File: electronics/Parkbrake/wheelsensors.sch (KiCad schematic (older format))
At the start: 61 parts

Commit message: ordernr, type and footprints for all components
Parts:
- C? (x2): footprint (none) -> Capacitors_SMD:C_0805; farnell (none) -> 2496940; part (none) -> 0805B104J500CT
- C? (x2): value 10n -> 1n; footprint (none) -> Capacitors_SMD:C_0805; farnell (none) -> 2494247; part (none) -> GRM2165C1H102JA01D
- C? (x2): footprint (none) -> Capacitors_SMD:c_elec_5x5.3; symbol C -> CP; farnell (none) -> 1870621; part (none) -> MCESL35V106M5X5.2
- C? (x4): footprint (none) -> Capacitors_SMD:C_0805; farnell (none) -> 2496981; part (none) -> 0805B473J500CT
- C? (x14): footprint (none) -> Capacitors_SMD:C_1206; farnell (none) -> 2362126; part (none) -> GRM31MR71E105JA01L
- Q?: value Q_PMOS_GSD -> BSS308; footprint (none) -> TO_SOT_Packages_SMD:SOT-23; farnell (none) -> 2432719; part (none) -> BSS308PE H6327
- Q?: value BSS138 -> 2N7002; footprint SOT-23 -> TO_SOT_Packages_SMD:SOT-23; farnell (none) -> 1510761; part (none) -> 2N7002
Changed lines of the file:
@@
 F 0 "C?" H 9925 3525 50  0000 L CNN
 F 1 "100n" H 9925 3325 50  0000 L CNN
-F 2 "" H 9938 3275 50  0000 C CNN
+F 2 "Capacitors_SMD:C_0805" H 9938 3275 50  0001 C CNN
 F 3 "" H 9900 3425 50  0000 C CNN
+F 4 "0805B104J500CT" H 9900 3425 60  0001 C CNN "part"
+F 5 "2496940" H 9900 3425 60  0001 C CNN "farnell"
 	1    9900 3425
 	1    0    0    -1
@@
 P 10150 3425
 F 0 "C?" H 10175 3525 50  0000 L CNN
-F 1 "10n" H 10175 3325 50  0000 L CNN
-F 2 "" H 10188 3275 50  0000 C CNN
+F 1 "1n" H 10175 3325 50  0000 L CNN
+F 2 "Capacitors_SMD:C_0805" H 10188 3275 50  0001 C CNN
 F 3 "" H 10150 3425 50  0000 C CNN
+F 4 "GRM2165C1H102JA01D" H 10150 3425 60  0001 C CNN "part"
+F 5 "2494247" H 10150 3425 60  0001 C CNN "farnell"
 	1    10150 3425
 	1    0    0    -1
 $EndComp
 $Comp
-L C C?
+L CP C?
 U 1 1 579010A2
 P 9650 3425
 F 0 "C?" H 9675 3525 50  0000 L CNN
 F 1 "10u" H 9675 3325 50  0000 L CNN
-F 2 "" H 9688 3275 50  0000 C CNN
+F 2 "Capacitors_SMD:c_elec_5x5.3" H 9688 3275 50  0001 C CNN
 F 3 "" H 9650 3425 50  0000 C CNN
+F 4 "1870621" H 9650 3425 60  0001 C CNN "farnell"
+F 5 "MCESL35V106M5X5.2" H 9650 3425 60  0001 C CNN "part"
 	1    9650 3425
 	1    0    0    -1
@@
 F 0 "C?" H 6950 3150 50  0000 L CNN
 F 1 "47n" H 6950 2950 50  0000 L CNN
-F 2 "" H 6963 2900 50  0000 C CNN
+F 2 "Capacitors_SMD:C_0805" H 6963 2900 50  0001 C CNN
 F 3 "" H 6925 3050 50  0000 C CNN
+F 4 "0805B473J500CT" H 6925 3050 60  0001 C CNN "part"
+F 5 "2496981" H 6925 3050 60  0001 C CNN "farnell"
 	1    6925 3050
 	1    0    0    -1
@@
 F 0 "C?" H 7225 3150 50  0000 L CNN
 F 1 "47n" H 7225 2950 50  0000 L CNN
-F 2 "" H 7238 2900 50  0000 C CNN
+F 2 "Capacitors_SMD:C_0805" H 7238 2900 50  0001 C CNN
 F 3 "" H 7200 3050 50  0000 C CNN
+F 4 "0805B473J500CT" H 7200 3050 60  0001 C CNN "part"
+F 5 "2496981" H 7200 3050 60  0001 C CNN "farnell"
 	1    7200 3050
 	1    0    0    -1
@@
 P 10075 4775
 F 0 "Q?" V 10300 4600 50  0000 R CNN
-F 1 "Q_PMOS_GSD" V 10425 5000 50  0000 R CNN
-F 2 "" H 10275 4875 50  0000 C CNN
+F 1 "BSS308" V 10300 4975 50  0000 R CNN
+F 2 "TO_SOT_Packages_SMD:SOT-23" H 10275 4875 50  0001 C CNN
 F 3 "" H 10075 4775 50  0000 C CNN
+F 4 "BSS308PE H6327" V 10075 4775 60  0001 C CNN "part"
+F 5 "2432719" V 10075 4775 60  0001 C CNN "farnell"
 	1    10075 4775
 	0    1    -1   0
@@
 P 9975 5325
 F 0 "Q?" H 10175 5400 50  0000 L CNN
-F 1 "BSS138" H 10175 5325 50  0000 L CNN
-F 2 "SOT-23" H 10175 5250 50  0000 L CIN
+F 1 "2N7002" H 10175 5325 50  0000 L CNN
+F 2 "TO_SOT_Packages_SMD:SOT-23" H 10175 5250 50  0001 L CIN
 F 3 "" H 9975 5325 50  0000 L CNN
+F 4 "1510761" H 9975 5325 60  0001 C CNN "farnell"
+F 5 "2N7002" H 9975 5325 60  0001 C CNN "part"
 	1    9975 5325
 	1    0    0    -1
@@
 F 0 "C?" H 9875 2125 50  0000 L CNN
 F 1 "100n" H 9875 1925 50  0000 L CNN
-F 2 "" H 9888 1875 50  0000 C CNN
+F 2 "Capacitors_SMD:C_0805" H 9888 1875 50  0001 C CNN
 F 3 "" H 9850 2025 50  0000 C CNN
+F 4 "0805B104J500CT" H 9850 2025 60  0001 C CNN "part"
+F 5 "2496940" H 9850 2025 60  0001 C CNN "farnell"
 	1    9850 2025
 	1    0    0    -1
@@
 P 10100 2025
 F 0 "C?" H 10125 2125 50  0000 L CNN
-F 1 "10n" H 10125 1925 50  0000 L CNN
-F 2 "" H 10138 1875 50  0000 C CNN
+F 1 "1n" H 10125 1925 50  0000 L CNN
+F 2 "Capacitors_SMD:C_0805" H 10138 1875 50  0001 C CNN
 F 3 "" H 10100 2025 50  0000 C CNN
+F 4 "GRM2165C1H102JA01D" H 10100 2025 60  0001 C CNN "part"
+F 5 "2494247" H 10100 2025 60  0001 C CNN "farnell"
 	1    10100 2025
 	1    0    0    -1
 $EndComp
 $Comp
-L C C?
+L CP C?
 U 1 1 579039C6
 P 9600 2025
 F 0 "C?" H 9625 2125 50  0000 L CNN
 F 1 "10u" H 9625 1925 50  0000 L CNN
-F 2 "" H 9638 1875 50  0000 C CNN
+F 2 "Capacitors_SMD:c_elec_5x5.3" H 9638 1875 50  0001 C CNN
 F 3 "" H 9600 2025 50  0000 C CNN
+F 4 "1870621" H 9600 2025 60  0001 C CNN "farnell"
+F 5 "MCESL35V106M5X5.2" H 9600 2025 60  0001 C CNN "part"
 	1    9600 2025
 	1    0    0    -1
@@
 F 0 "C?" H 6950 1825 50  0000 L CNN
 F 1 "47n" H 6950 1625 50  0000 L CNN
-F 2 "" H 6963 1575 50  0000 C CNN
+F 2 "Capacitors_SMD:C_0805" H 6963 1575 50  0001 C CNN
 F 3 "" H 6925 1725 50  0000 C CNN
+F 4 "0805B473J500CT" H 6925 1725 60  0001 C CNN "part"
+F 5 "2496981" H 6925 1725 60  0001 C CNN "farnell"
 	1    6925 1725
 	1    0    0    -1
@@
 F 0 "C?" H 7225 1825 50  0000 L CNN
 F 1 "47n" H 7225 1625 50  0000 L CNN
-F 2 "" H 7238 1575 50  0000 C CNN
+F 2 "Capacitors_SMD:C_0805" H 7238 1575 50  0001 C CNN
 F 3 "" H 7200 1725 50  0000 C CNN
+F 4 "0805B473J500CT" H 7200 1725 60  0001 C CNN "part"
+F 5 "2496981" H 7200 1725 60  0001 C CNN "farnell"
 	1    7200 1725
 	1    0    0    -1
@@
 F 0 "C?" H 3250 5200 50  0000 L CNN
 F 1 "1u" H 3250 5000 50  0000 L CNN
-F 2 "" H 3263 4950 50  0000 C CNN
+F 2 "Capacitors_SMD:C_1206" H 3263 4950 50  0001 C CNN
 F 3 "" H 3225 5100 50  0000 C CNN
+F 4 "2362126" H 3225 5100 60  0001 C CNN "farnell"
+F 5 "GRM31MR71E105JA01L" H 3225 5100 60  0001 C CNN "part"
 	1    3225 5100
 	1    0    0    -1
@@
 F 0 "C?" H 3100 5450 50  0000 L CNN
 F 1 "1u" H 3100 5250 50  0000 L CNN
-F 2 "" H 3113 5200 50  0000 C CNN
+F 2 "Capacitors_SMD:C_1206" H 3113 5200 50  0001 C CNN
 F 3 "" H 3075 5350 50  0000 C CNN
+F 4 "2362126" H 3075 5350 60  0001 C CNN "farnell"
+F 5 "GRM31MR71E105JA01L" H 3075 5350 60  0001 C CNN "part"
 	1    3075 5350
 	0    1    1    0
@@
 F 0 "C?" H 3100 5950 50  0000 L CNN
 F 1 "1u" H 3100 5750 50  0000 L CNN
-F 2 "" H 3113 5700 50  0000 C CNN
+F 2 "Capacitors_SMD:C_1206" H 3113 5700 50  0001 C CNN
 F 3 "" H 3075 5850 50  0000 C CNN
+F 4 "2362126" H 3075 5850 60  0001 C CNN "farnell"
+F 5 "GRM31MR71E105JA01L" H 3075 5850 60  0001 C CNN "part"
 	1    3075 5850
 	0    1    1    0
@@
 F 0 "C?" H 1600 5250 50  0000 L CNN
 F 1 "1u" H 1600 5050 50  0000 L CNN
-F 2 "" H 1613 5000 50  0000 C CNN
+F 2 "Capacitors_SMD:C_1206" H 1613 5000 50  0001 C CNN
 F 3 "" H 1575 5150 50  0000 C CNN
+F 4 "2362126" H 1575 5150 60  0001 C CNN "farnell"
+F 5 "GRM31MR71E105JA01L" H 1575 5150 60  0001 C CNN "part"
 	1    1575 5150
 	1    0    0    -1
@@
 F 0 "C?" H 1600 5750 50  0000 L CNN
 F 1 "1u" H 1600 5550 50  0000 L CNN
-F 2 "" H 1613 5500 50  0000 C CNN
+F 2 "Capacitors_SMD:C_1206" H 1613 5500 50  0001 C CNN
 F 3 "" H 1575 5650 50  0000 C CNN
+F 4 "2362126" H 1575 5650 60  0001 C CNN "farnell"
+F 5 "GRM31MR71E105JA01L" H 1575 5650 60  0001 C CNN "part"
 	1    1575 5650
 	1    0    0    -1
@@
 F 0 "C?" H 3150 6400 50  0000 L CNN
 F 1 "1u" H 3150 6200 50  0000 L CNN
-F 2 "" H 3163 6150 50  0000 C CNN
+F 2 "Capacitors_SMD:C_1206" H 3163 6150 50  0001 C CNN
 F 3 "" H 3125 6300 50  0000 C CNN
+F 4 "2362126" H 3125 6300 60  0001 C CNN "farnell"
+F 5 "GRM31MR71E105JA01L" H 3125 6300 60  0001 C CNN "part"
 	1    3125 6300
 	1    0    0    -1
@@
 F 0 "C?" H 3375 6400 50  0000 L CNN
 F 1 "1u" H 3375 6200 50  0000 L CNN
-F 2 "" H 3388 6150 50  0000 C CNN
+F 2 "Capacitors_SMD:C_1206" H 3388 6150 50  0001 C CNN
 F 3 "" H 3350 6300 50  0000 C CNN
+F 4 "2362126" H 3350 6300 60  0001 C CNN "farnell"
+F 5 "GRM31MR71E105JA01L" H 3350 6300 60  0001 C CNN "part"
 	1    3350 6300
 	1    0    0    -1
@@
 F 0 "C?" H 6300 5200 50  0000 L CNN
 F 1 "1u" H 6300 5000 50  0000 L CNN
-F 2 "" H 6313 4950 50  0000 C CNN
+F 2 "Capacitors_SMD:C_1206" H 6313 4950 50  0001 C CNN
 F 3 "" H 6275 5100 50  0000 C CNN
+F 4 "2362126" H 6275 5100 60  0001 C CNN "farnell"
+F 5 "GRM31MR71E105JA01L" H 6275 5100 60  0001 C CNN "part"
 	1    6275 5100
 	1    0    0    -1
@@
 F 0 "C?" H 6150 5450 50  0000 L CNN
 F 1 "1u" H 6150 5250 50  0000 L CNN
-F 2 "" H 6163 5200 50  0000 C CNN
+F 2 "Capacitors_SMD:C_1206" H 6163 5200 50  0001 C CNN
 F 3 "" H 6125 5350 50  0000 C CNN
+F 4 "2362126" H 6125 5350 60  0001 C CNN "farnell"
+F 5 "GRM31MR71E105JA01L" H 6125 5350 60  0001 C CNN "part"
 	1    6125 5350
 	0    1    1    0
@@
 F 0 "C?" H 6150 5950 50  0000 L CNN
 F 1 "1u" H 6150 5750 50  0000 L CNN
-F 2 "" H 6163 5700 50  0000 C CNN
+F 2 "Capacitors_SMD:C_1206" H 6163 5700 50  0001 C CNN
 F 3 "" H 6125 5850 50  0000 C CNN
+F 4 "2362126" H 6125 5850 60  0001 C CNN "farnell"
+F 5 "GRM31MR71E105JA01L" H 6125 5850 60  0001 C CNN "part"
 	1    6125 5850
 	0    1    1    0
@@
 F 0 "C?" H 4650 5250 50  0000 L CNN
 F 1 "1u" H 4650 5050 50  0000 L CNN
-F 2 "" H 4663 5000 50  0000 C CNN
+F 2 "Capacitors_SMD:C_1206" H 4663 5000 50  0001 C CNN
 F 3 "" H 4625 5150 50  0000 C CNN
+F 4 "2362126" H 4625 5150 60  0001 C CNN "farnell"
+F 5 "GRM31MR71E105JA01L" H 4625 5150 60  0001 C CNN "part"
 	1    4625 5150
 	1    0    0    -1
@@
 F 0 "C?" H 4650 5750 50  0000 L CNN
 F 1 "1u" H 4650 5550 50  0000 L CNN
-F 2 "" H 4663 5500 50  0000 C CNN
+F 2 "Capacitors_SMD:C_1206" H 4663 5500 50  0001 C CNN
 F 3 "" H 4625 5650 50  0000 C CNN
+F 4 "2362126" H 4625 5650 60  0001 C CNN "farnell"
+F 5 "GRM31MR71E105JA01L" H 4625 5650 60  0001 C CNN "part"
 	1    4625 5650
 	1    0    0    -1
@@
 F 0 "C?" H 6200 6400 50  0000 L CNN
 F 1 "1u" H 6200 6200 50  0000 L CNN
-F 2 "" H 6213 6150 50  0000 C CNN
+F 2 "Capacitors_SMD:C_1206" H 6213 6150 50  0001 C CNN
 F 3 "" H 6175 6300 50  0000 C CNN
+F 4 "2362126" H 6175 6300 60  0001 C CNN "farnell"
+F 5 "GRM31MR71E105JA01L" H 6175 6300 60  0001 C CNN "part"
 	1    6175 6300
 	1    0    0    -1
@@
 F 0 "C?" H 6425 6400 50  0000 L CNN
 F 1 "1u" H 6425 6200 50  0000 L CNN
-F 2 "" H 6438 6150 50  0000 C CNN
+F 2 "Capacitors_SMD:C_1206" H 6438 6150 50  0001 C CNN
 F 3 "" H 6400 6300 50  0000 C CNN
+F 4 "2362126" H 6400 6300 60  0001 C CNN "farnell"
+F 5 "GRM31MR71E105JA01L" H 6400 6300 60  0001 C CNN "part"
 	1    6400 6300
 	1    0    0    -1

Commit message: Make it pass DRC rule check
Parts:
- gave numbers to parts that had none: 61

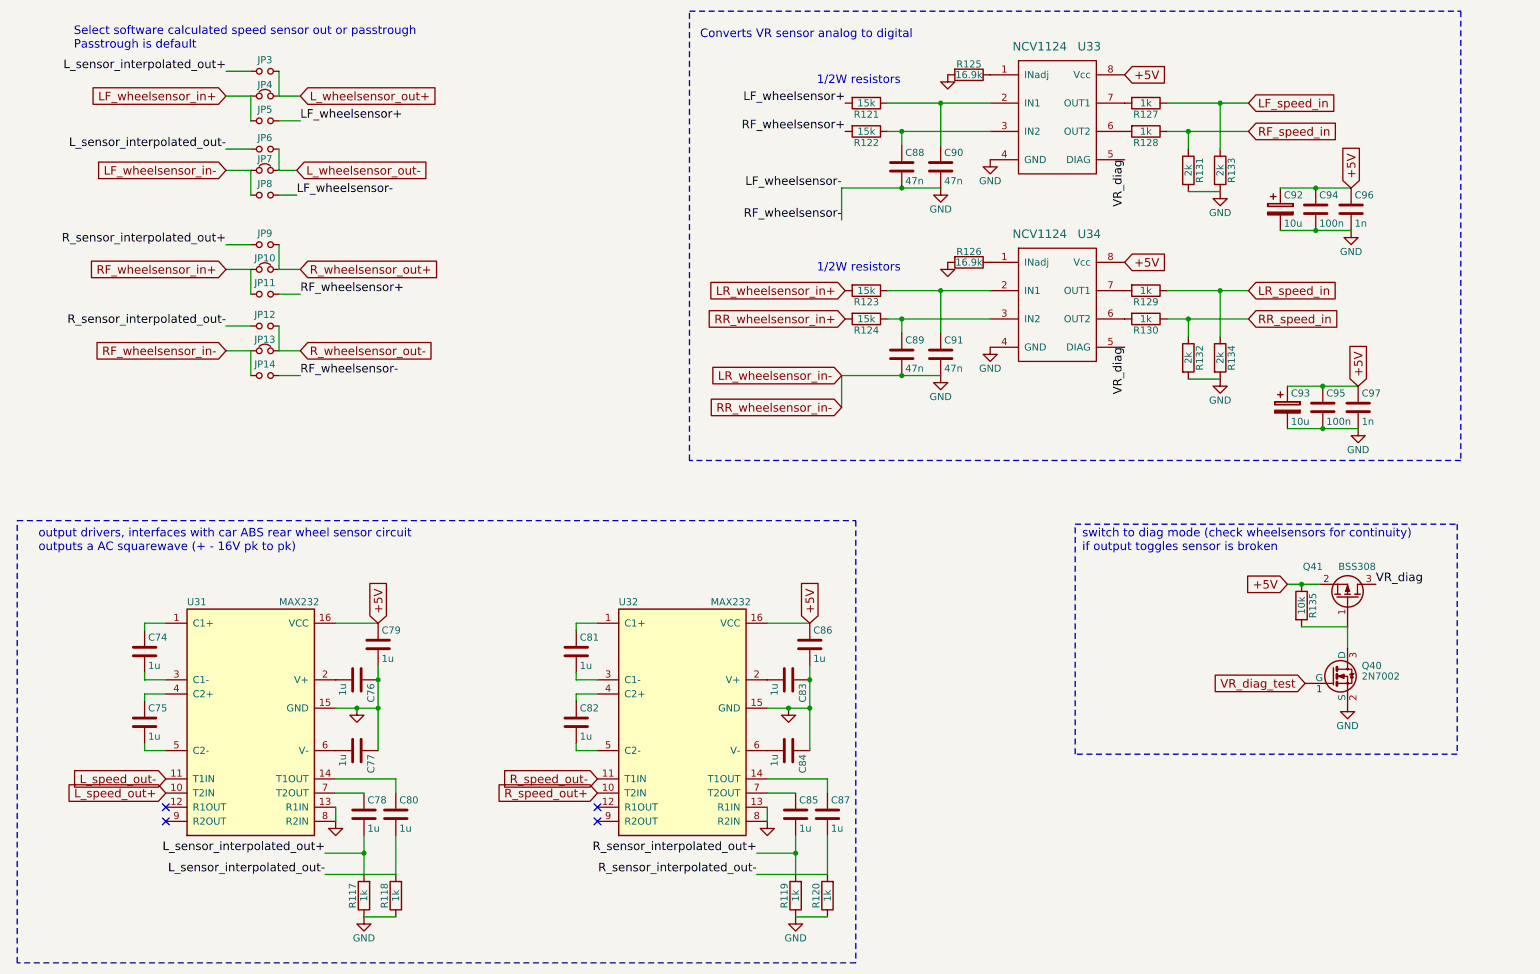
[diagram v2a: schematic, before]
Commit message: More fixes and chenged components eat less boardspace
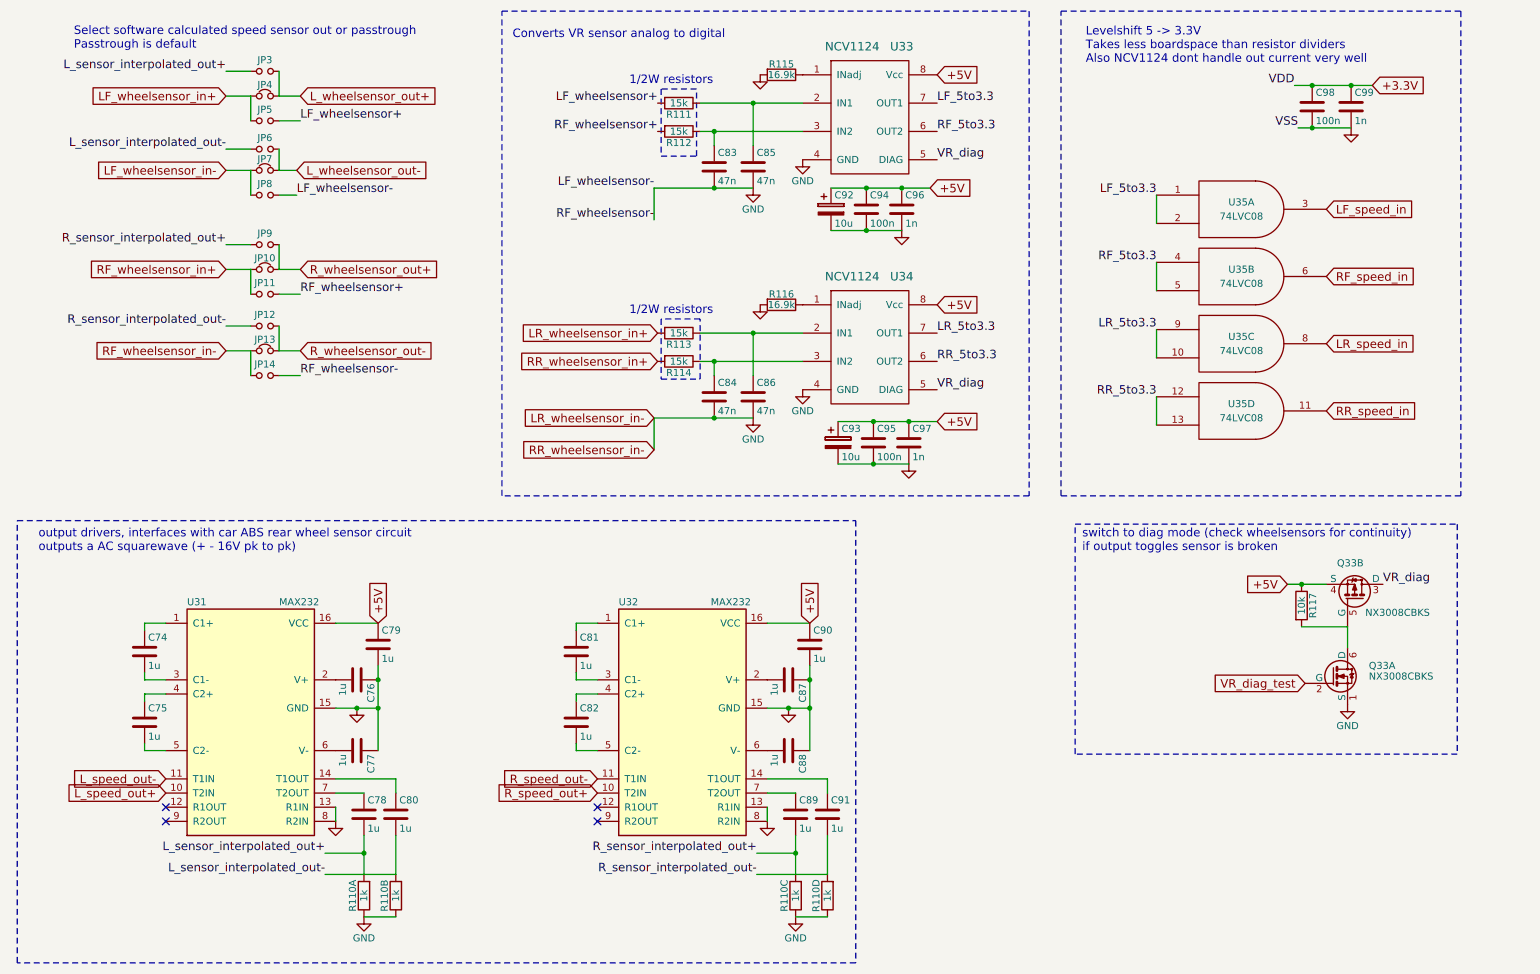
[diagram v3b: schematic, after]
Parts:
- removed Q40: 2N7002, TO_SOT_Packages_SMD:SOT-23, symbol BSS138
- removed Q41: BSS308, TO_SOT_Packages_SMD:SOT-23, symbol Q_PMOS_GSD
- removed R117, R118, R119, R120, R127, R128, R129, R130: 1k, Resistors_SMD:R_0805, symbol R
- removed R131, R132, R133, R134: 2k, Resistors_SMD:R_0805, symbol R
- added C98: 100n, Capacitors_SMD:C_0805, symbol C
- added C99: 1n, Capacitors_SMD:C_0805, symbol C
- added Q33: NX3008CBKS, SOT363:SOT-363, symbol NX3008CBKS
- added R110: 1k, Resistors_SMD:R_Array_Concave_4x0603, symbol Rnet4
- added U35: 74LVC08, Housings_SSOP:TSSOP-14_4.4x5mm_Pitch0.65mm, symbol 74LS08
- C92, C93: footprint Capacitors_SMD:c_elec_5x5.3 -> myfootprints:CP_0805; farnell 1870621 -> 2491430; part MCESL35V106M5X5.2 -> TMCP0J106KTRF
- JP10: value Jumper_NC_Small -> RF_passth+; footprint (none) -> Resistors_SMD:R_0805_HandSoldering; farnell (none) -> 9240276; part (none) -> RC1206JR-070RL
- JP11: value Jumper_NO_Small -> RF+_to_in; footprint (none) -> Resistors_SMD:R_0805_HandSoldering; farnell (none) -> 9240276; part (none) -> RC1206JR-070RL
- JP12: value Jumper_NO_Small -> soft_R_out-; footprint (none) -> Resistors_SMD:R_0805_HandSoldering; farnell (none) -> 9240276; part (none) -> RC1206JR-070RL
- JP13: value Jumper_NC_Small -> RF_passth-; footprint (none) -> Resistors_SMD:R_0805_HandSoldering; farnell (none) -> 9240276; part (none) -> RC1206JR-070RL
- JP14: value Jumper_NO_Small -> RF-_to_in; footprint (none) -> Resistors_SMD:R_0805_HandSoldering; farnell (none) -> 9240276; part (none) -> RC1206JR-070RL
- JP3: value Jumper_NO_Small -> soft_L_out+; footprint (none) -> Resistors_SMD:R_0805_HandSoldering; farnell (none) -> 9240276; part (none) -> RC1206JR-070RL
- JP4: value Jumper_NC_Small -> L_passth+; footprint (none) -> Resistors_SMD:R_0805_HandSoldering; farnell (none) -> 9240276; part (none) -> RC1206JR-070RL
- JP5: value Jumper_NO_Small -> LF+_to_in; footprint (none) -> Resistors_SMD:R_0805_HandSoldering; farnell (none) -> 9240276; part (none) -> RC1206JR-070RL
- JP6: value Jumper_NO_Small -> soft_L_out-; footprint (none) -> Resistors_SMD:R_0805_HandSoldering; farnell (none) -> 9240276; part (none) -> RC1206JR-070RL
- JP7: value Jumper_NC_Small -> L_passth-; footprint (none) -> Resistors_SMD:R_0805_HandSoldering; farnell (none) -> 9240276; part (none) -> RC1206JR-070RL
- JP8: value Jumper_NO_Small -> LF-_to_in; footprint (none) -> Resistors_SMD:R_0805_HandSoldering; farnell (none) -> 9240276; part (none) -> RC1206JR-070RL
- JP9: value Jumper_NO_Small -> soft_R_out+; footprint (none) -> Resistors_SMD:R_0805_HandSoldering; farnell (none) -> 9240276; part (none) -> RC1206JR-070RL
- R111: renamed from R121; farnell 9332618 -> 1750772; part MC01W0805115K -> ERJP06F1502V
- R112: renamed from R122; farnell 9332618 -> 1750772; part MC01W0805115K -> ERJP06F1502V
- R113: renamed from R123; farnell 9332618 -> 1750772; part MC01W0805115K -> ERJP06F1502V
- R114: renamed from R124; farnell 9332618 -> 1750772; part MC01W0805115K -> ERJP06F1502V
- renumbered C88 to C83, C89 to C84, C90 to C85, C91 to C86, C83 to C87, C84 to C88, C85 to C89, C86 to C90, C87 to C91, R125 to R115, R126 to R116, R135 to R117
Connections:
- net +5V: now also Q33.4 (S)
- net GND: now also C98.2, C99.2, Q33.1 (S), R110.1, R110.2, R110.3, R110.4, U35.7 (GND), U35.7 (GND), U35.7 (GND), U35.7 (GND)
- net LF_speed_in: now also U35.3
- net LR_speed_in: now also U35.8
- net L_sensor_interpolated_out+: now also R110.8
- net L_sensor_interpolated_out-: now also R110.7
- net RF_speed_in: now also U35.6
- net RR_speed_in: now also U35.11
- net R_sensor_interpolated_out+: now also R110.6
- net R_sensor_interpolated_out-: now also R110.5
- net VR_diag: now also Q33.3 (D)
- net VR_diag_test: now also Q33.2 (G)
- net RR_5to3.3: now reaches U34.6 (OUT2)
- net RR_5to3.3: now also U35.12, U35.13
- net LR_5to3.3: now reaches U34.7 (OUT1)
- net LR_5to3.3: now also U35.10, U35.9
- net at R117.2: now also Q33.5 (G), Q33.6 (D)
- net RF_5to3.3: now reaches U33.6 (OUT2)
- net RF_5to3.3: now also U35.4, U35.5
- net LF_5to3.3: now reaches U33.7 (OUT1)
- net LF_5to3.3: now also U35.1, U35.2
- new net +3.3V: C98.1, C99.1
- new net VCC: U35.14 (VCC), U35.14 (VCC), U35.14 (VCC), U35.14 (VCC)
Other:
- note added: "Levelshift 5 -> 3.3V\nTakes less boardspace than resistor dividers\nAlso NCV1124 dont handle out current very well"
- moved on the sheet: C83, C84, C85, C86, C92, C93, C94, C95, C96, C97, R111, R112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
